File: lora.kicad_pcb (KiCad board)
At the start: 4 copper layers, 80.5 x 45 mm, 51 parts, among them J11 Conn_Coaxial, J2 Humidity, J3 Temp, J5 Temp, J6 VDD, J7 GPS, J8 SIM800, J9 I2C, Q1 AO3401A, Q2 AO3401A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

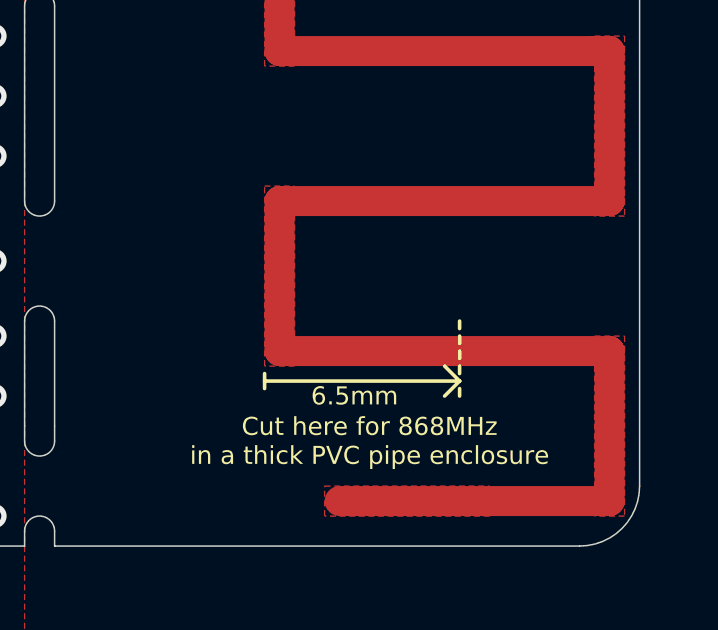
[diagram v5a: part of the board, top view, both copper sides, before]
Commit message: added label for antenna length
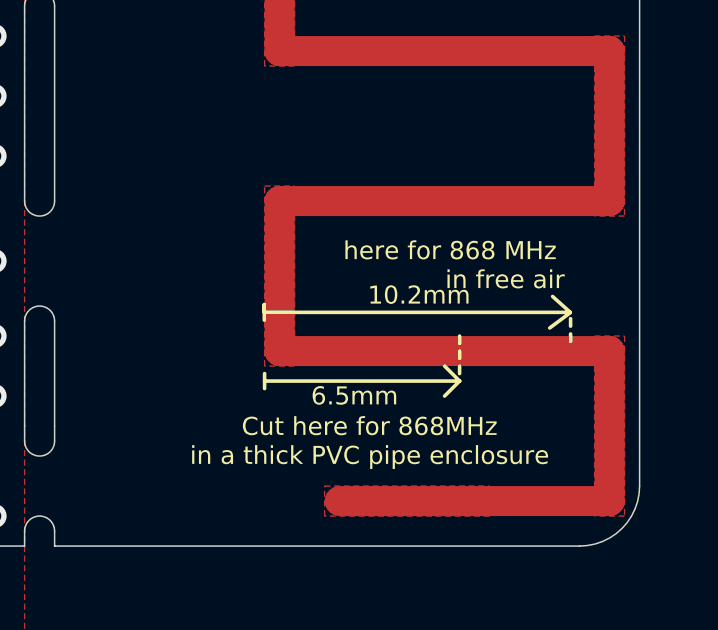
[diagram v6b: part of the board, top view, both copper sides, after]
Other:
- board text added: "10.2mm"
- board text added: "here for 868 MHz in free air"
